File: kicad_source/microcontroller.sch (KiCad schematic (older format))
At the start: 50 parts, among them CN1 MEM2061-01-188-00-A, CN2 FSH-105-04-L-DH-SL, CN5 CONN_01X14, CN6 CONN_01X04, SW1 PTS 647 SK38 SMTR2 LFS, SW2 TAST_VER, SW3 PTS636 SL43 SMTR LFS, SW4 PTS 647 SK38 SMTR2 LFS, U1 W25Q80D, U2 ATECC608A, U3 FE310-G002, U8 BMA253, Y1 FA-238 16.0000MB-C3

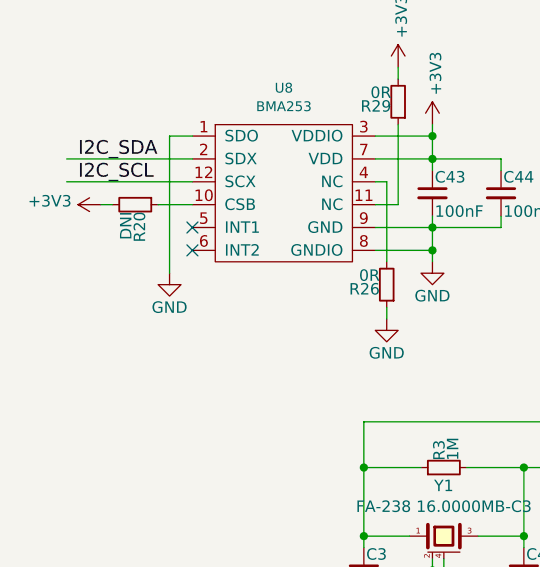
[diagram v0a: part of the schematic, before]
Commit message: connected interrupt line of BMA253, updated layout
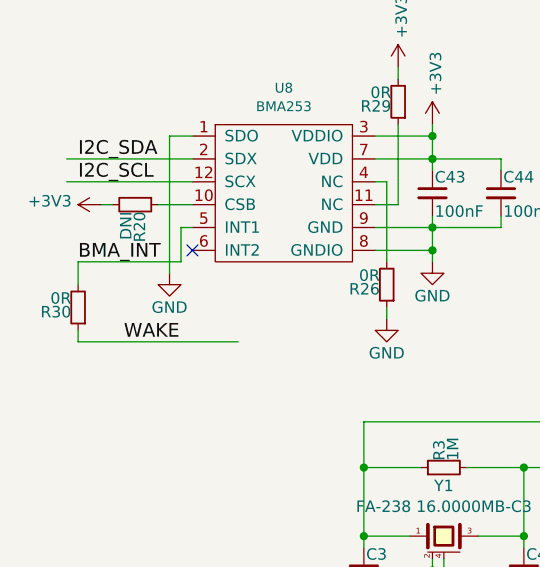
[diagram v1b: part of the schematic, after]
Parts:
- added R30: 0R, resistors:R_0603, symbol devices:R_1206
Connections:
- net labels added: BMA_INT
- wire segments 252 -> 258
- no-connect marks 12 -> 11
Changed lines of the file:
@@
 Wire Wire Line
 	2300 1150 2300 1050
-NoConn ~ 1250 1450
 NoConn ~ 1250 1550
 $Comp
@@
 Wire Wire Line
 	2150 800  2150 750
+$Comp
+L devices:R_1206 R30
+U 1 1 5EE92263
+P 750 1800
+F 0 "R30" H 780 1820 50  0000 L CNN
+F 1 "0R" H 780 1760 50  0000 L CNN
+F 2 "resistors:R_0603" H 750 1650 50  0001 C CNN
+F 3 "" H 750 1800 50  0000 C CNN
+	1    750  1800
+	-1   0    0    1
+$EndComp
+Wire Wire Line
+	1250 1450 1200 1450
+Wire Wire Line
+	1200 1450 1200 1600
+Wire Wire Line
+	1200 1600 750  1600
+Wire Wire Line
+	750  1600 750  1700
+Wire Wire Line
+	1450 1950 750  1950
+Wire Wire Line
+	750  1950 750  1900
+Text Label 750  1600 0    60   ~ 0
+BMA_INT
+Text Label 950  1950 0    60   ~ 0
+WAKE
 $EndSCHEMATC

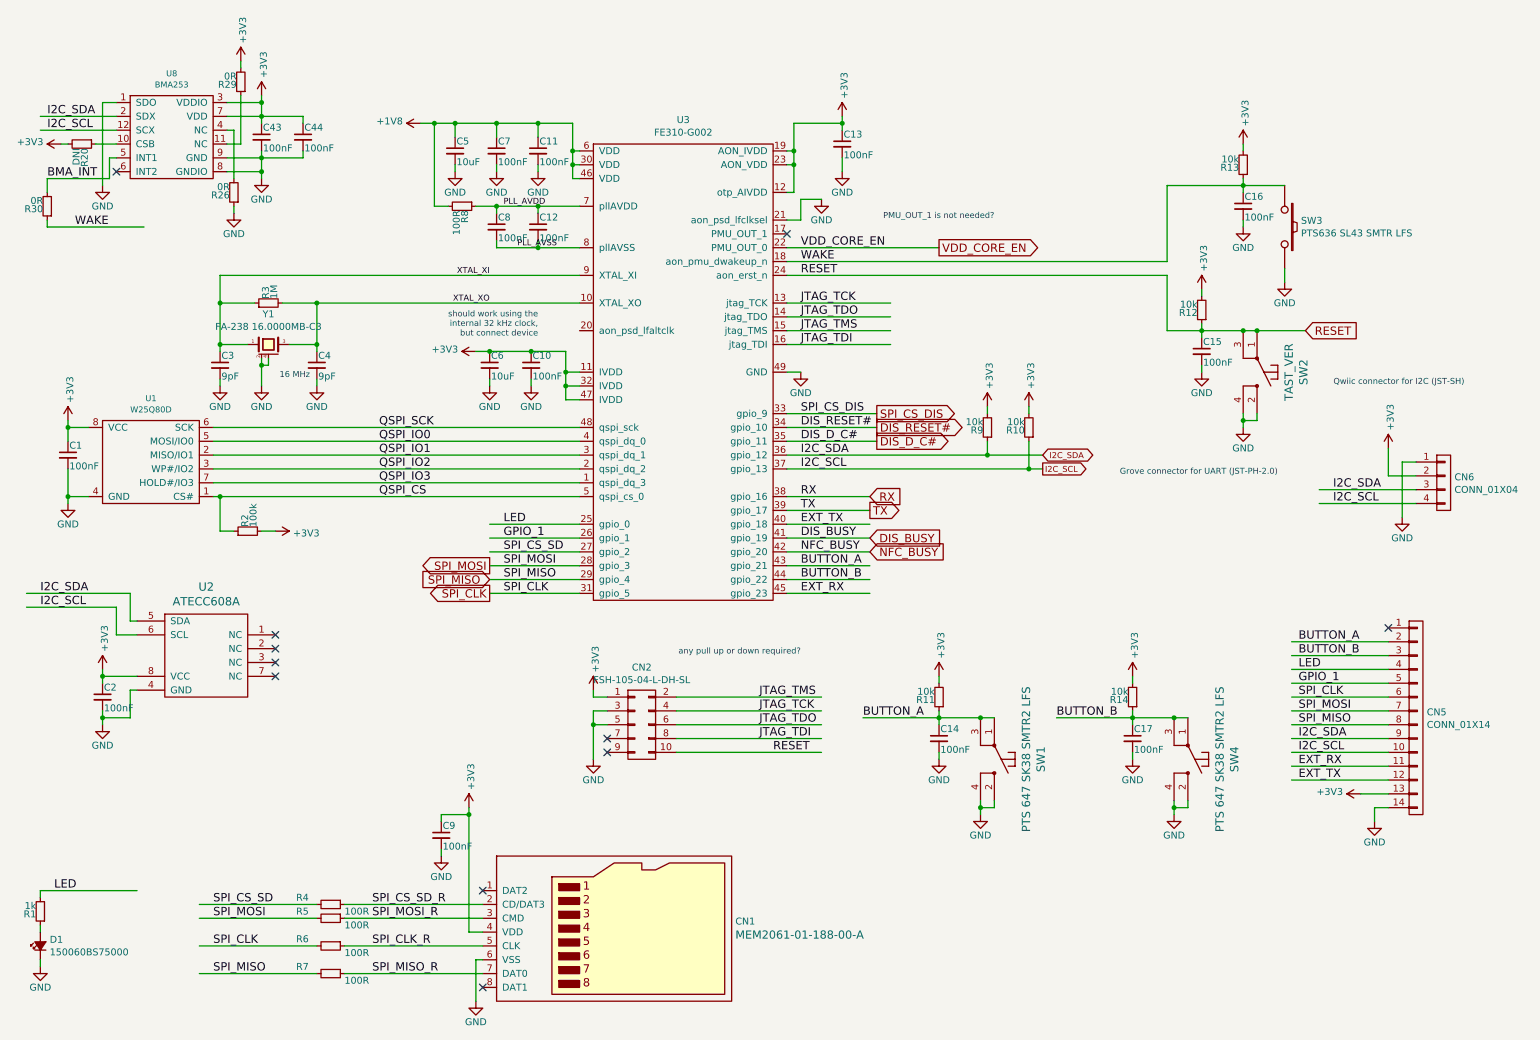
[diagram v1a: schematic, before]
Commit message: added test points, finished layout
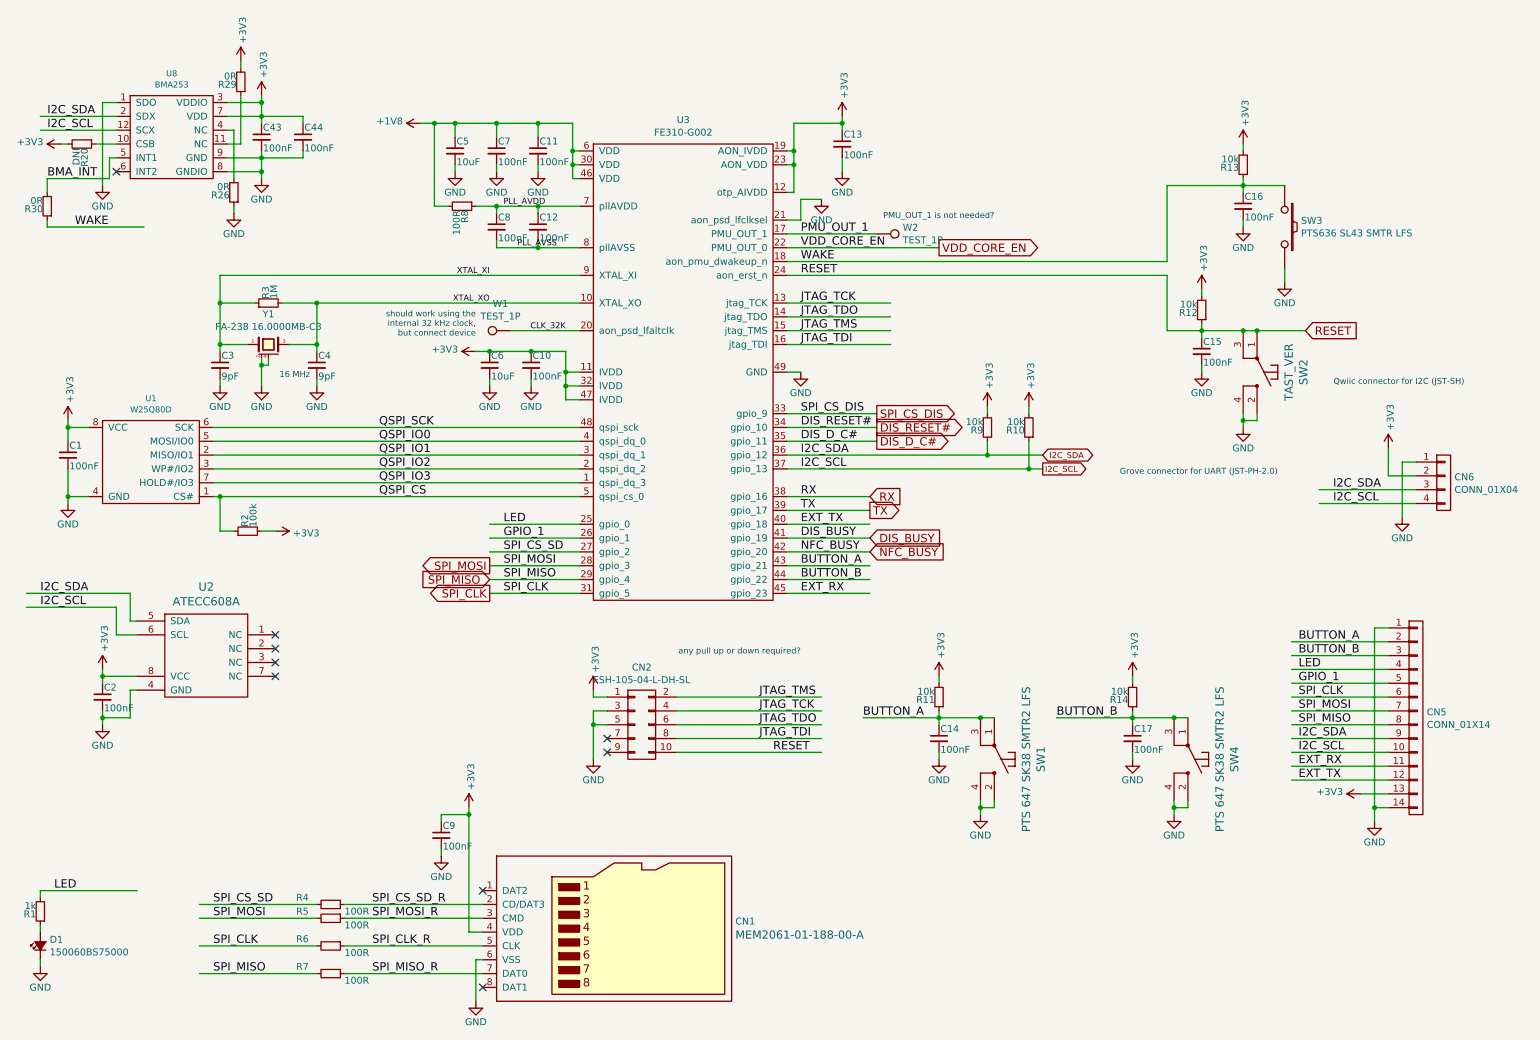
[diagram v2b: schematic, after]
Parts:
- added W1, W2: TEST_1P, wire_pads:SolderWirePad_single_1mmSMD, symbol mechanical-connectors:TEST_1P
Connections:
- net labels added: CLK_32K, PMU_OUT_1
- wire segments 258 -> 262
- no-connect marks 11 -> 9
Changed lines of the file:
@@
 Text Label 6200 2800 0    60   ~ 0
 JTAG_TDI
-Text Notes 4300 2750 2    43   ~ 0
+Text Notes 3850 2750 2    43   ~ 0
 should work using the \ninternal 32 kHz clock, \nbut connect device
 Text Notes 7600 1900 2    43   ~ 0
 PMU_OUT_1 is not needed?
-NoConn ~ 6100 2000
 Wire Wire Line
 	2700 2500 2700 2800
@@
 Text Label 4050 4200 0    60   ~ 0
 GPIO_1
-$Comp
-L mechanical-connectors:CONN_01X14 CN5
-U 1 1 5EE75FCC
-P 10650 5500
-F 0 "CN5" H 10728 5541 50  0000 L CNN
-F 1 "CONN_01X14" H 10728 5450 50  0000 L CNN
-F 2 "CON_samtec:SIB-114-02-F-S_MATING" H 10650 5500 50  0001 C CNN
-F 3 "" H 10650 5500 50  0000 C CNN
-	1    10650 5500
-	1    0    0    -1
-$EndComp
 Wire Wire Line
 	9750 5150 10450 5150
@@
 Text Label 9800 4950 0    60   ~ 0
 BUTTON_A
-NoConn ~ 10450 4850
 Wire Wire Line
 	9400 1650 9700 1650
@@
 Text Label 950  1950 0    60   ~ 0
 WAKE
+$Comp
+L mechanical-connectors:TEST_1P W1
+U 1 1 5EEC013D
+P 4100 2700
+F 0 "W1" V 4295 2772 50  0000 C CNN
+F 1 "TEST_1P" V 4204 2772 50  0000 C CNN
+F 2 "wire_pads:SolderWirePad_single_1mmSMD" H 4300 2700 50  0001 C CNN
+F 3 "" H 4300 2700 50  0000 C CNN
+	1    4100 2700
+	0    -1   -1   0
+$EndComp
+$Comp
+L mechanical-connectors:TEST_1P W2
+U 1 1 5EED793A
+P 6750 2000
+F 0 "W2" V 6704 2188 50  0000 L CNN
+F 1 "TEST_1P" V 6795 2188 50  0000 L CNN
+F 2 "wire_pads:SolderWirePad_single_1mmSMD" H 6950 2000 50  0001 C CNN
+F 3 "" H 6950 2000 50  0000 C CNN
+	1    6750 2000
+	0    1    1    0
+$EndComp
+Wire Wire Line
+	6750 2000 6100 2000
+Text Label 6200 2000 0    60   ~ 0
+PMU_OUT_1
+Wire Wire Line
+	4100 2700 4600 2700
+Text Label 4500 2700 2    43   ~ 0
+CLK_32K
+$Comp
+L mechanical-connectors:CONN_01X14 CN5
+U 1 1 5EE75FCC
+P 10650 5500
+F 0 "CN5" H 10728 5541 50  0000 L CNN
+F 1 "CONN_01X14" H 10728 5450 50  0000 L CNN
+F 2 "CON_samtec:SIB-114-02-F-S_MATING" H 10650 5500 50  0001 C CNN
+F 3 "" H 10650 5500 50  0000 C CNN
+	1    10650 5500
+	1    0    0    -1
+$EndComp
+Wire Wire Line
+	10450 4850 10350 4850
+Wire Wire Line
+	10350 4850 10350 6150
+Connection ~ 10350 6150
 $EndSCHEMATC

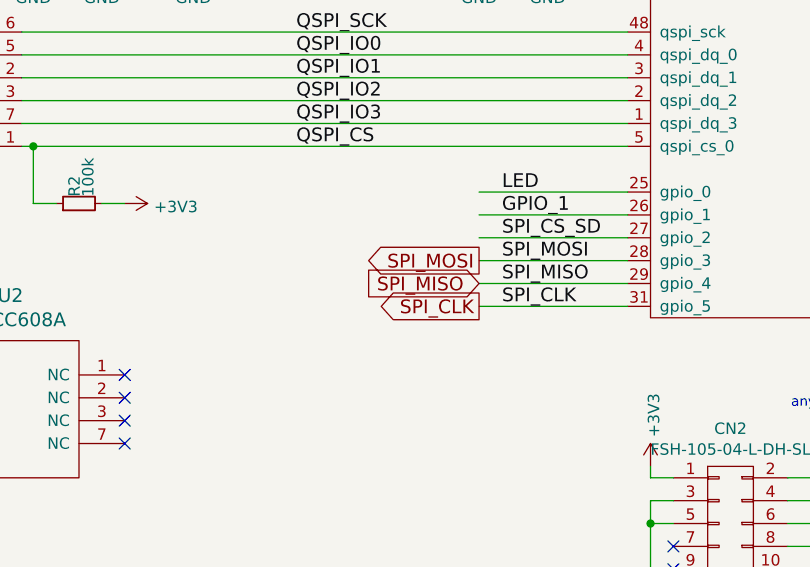
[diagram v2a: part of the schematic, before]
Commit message: added C45 to pin4 of display
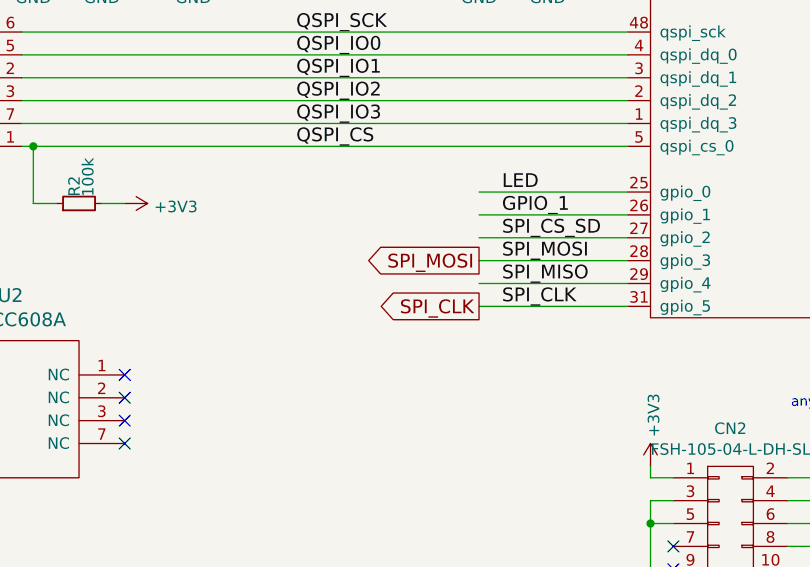
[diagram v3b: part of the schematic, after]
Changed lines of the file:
@@
 Sheet 2 7
 Title "Risc V FE310 microcontroller"
-Date "2020-05-13"
+Date "2020-07-03"
 Rev "dev_0.1"
 Comp "generationmake"
@@
 Text GLabel 3950 4400 0    60   Output ~ 0
 SPI_MOSI
-Text GLabel 3950 4500 0    60   Input ~ 0
-SPI_MISO
 Text GLabel 6750 3300 2    60   Output ~ 0
 SPI_CS_DIS

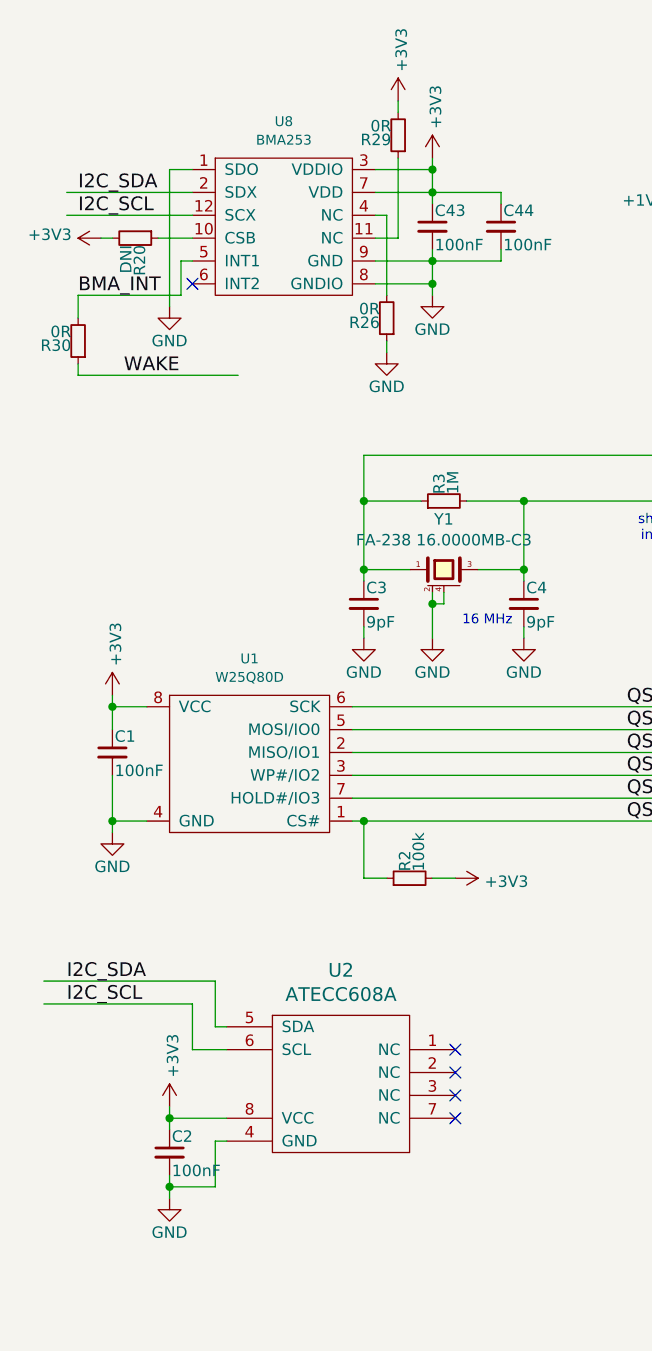
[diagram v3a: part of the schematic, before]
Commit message: added i2c addresses to schematic pdf and readme
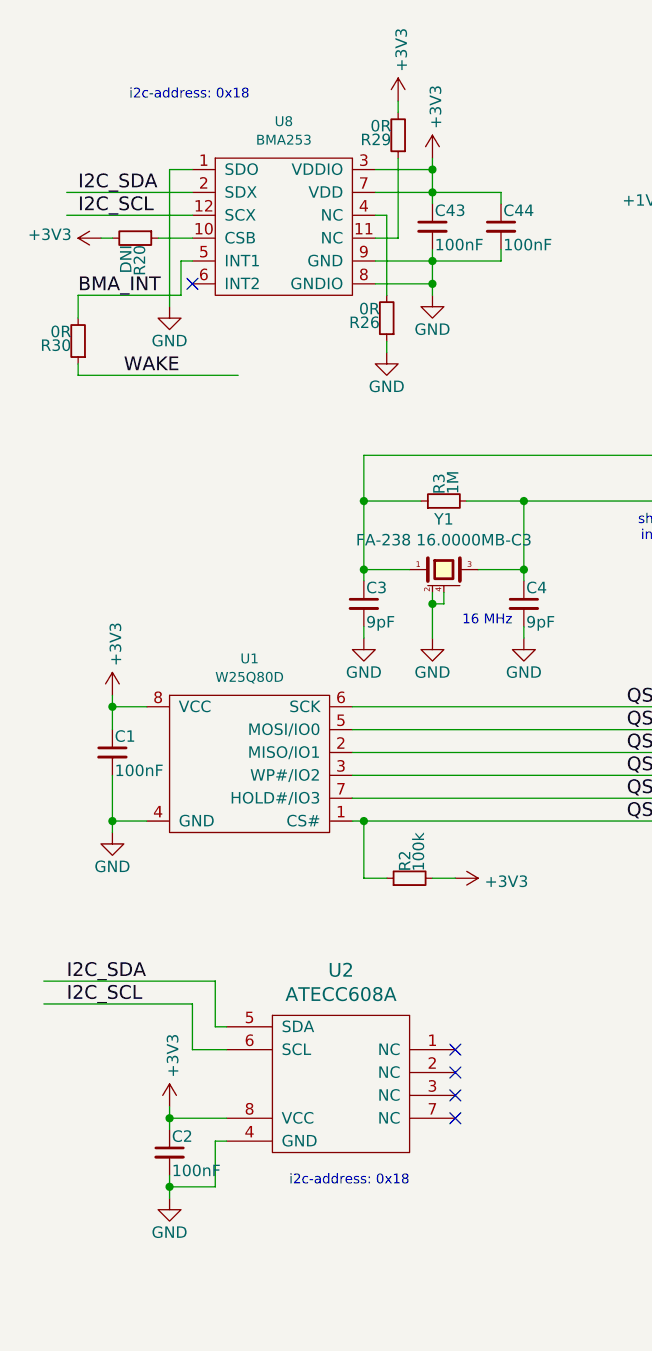
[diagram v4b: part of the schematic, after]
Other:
- note added: "i2c-address: 0x18"
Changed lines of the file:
@@
 Sheet 2 7
 Title "Risc V FE310 microcontroller"
-Date "2020-07-03"
-Rev "dev_0.1"
+Date "2020-07-10"
+Rev "0.1"
 Comp "generationmake"
 Comment1 ""
@@
 	10350 4850 10350 6150
 Connection ~ 10350 6150
+Text Notes 1500 750  2    43   ~ 0
+i2c-address: 0x18
+Text Notes 2200 5500 2    43   ~ 0
+i2c-address: 0x18
 $EndSCHEMATC

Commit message: added missing parts to 3d model, updated step file
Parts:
- SW3: footprint mechanical-switches:smd_push -> mechanical-switches:WE_434121050816
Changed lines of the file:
@@
 F 0 "SW3" V 9654 2068 50  0000 L CNN
 F 1 "PTS636 SL43 SMTR LFS " V 9745 2068 50  0000 L CNN
-F 2 "mechanical-switches:smd_push" V 9791 2068 50  0001 L CNN
+F 2 "mechanical-switches:WE_434121050816" V 9791 2068 50  0001 L CNN
 F 3 "" H 9700 1950 50  0000 C CNN
 	1    9700 1950
